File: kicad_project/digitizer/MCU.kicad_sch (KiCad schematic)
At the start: 27 parts, among them J401 Conn_02x05_Odd_Even, U401 ATSAM4E8EA-AN

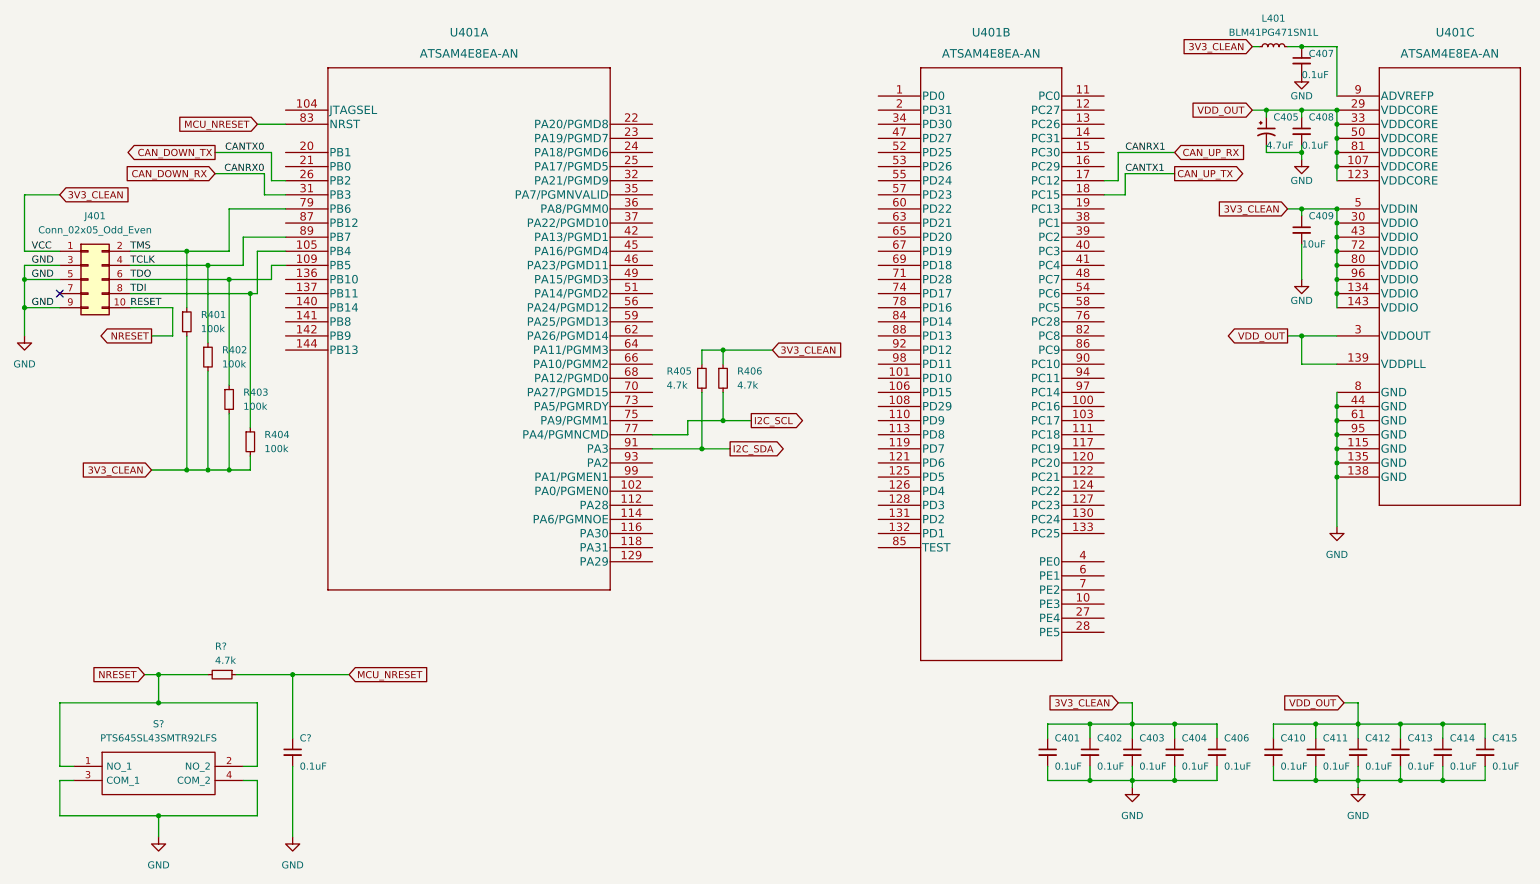
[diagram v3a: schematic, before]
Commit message: added GPIO lines, LED, other small changes
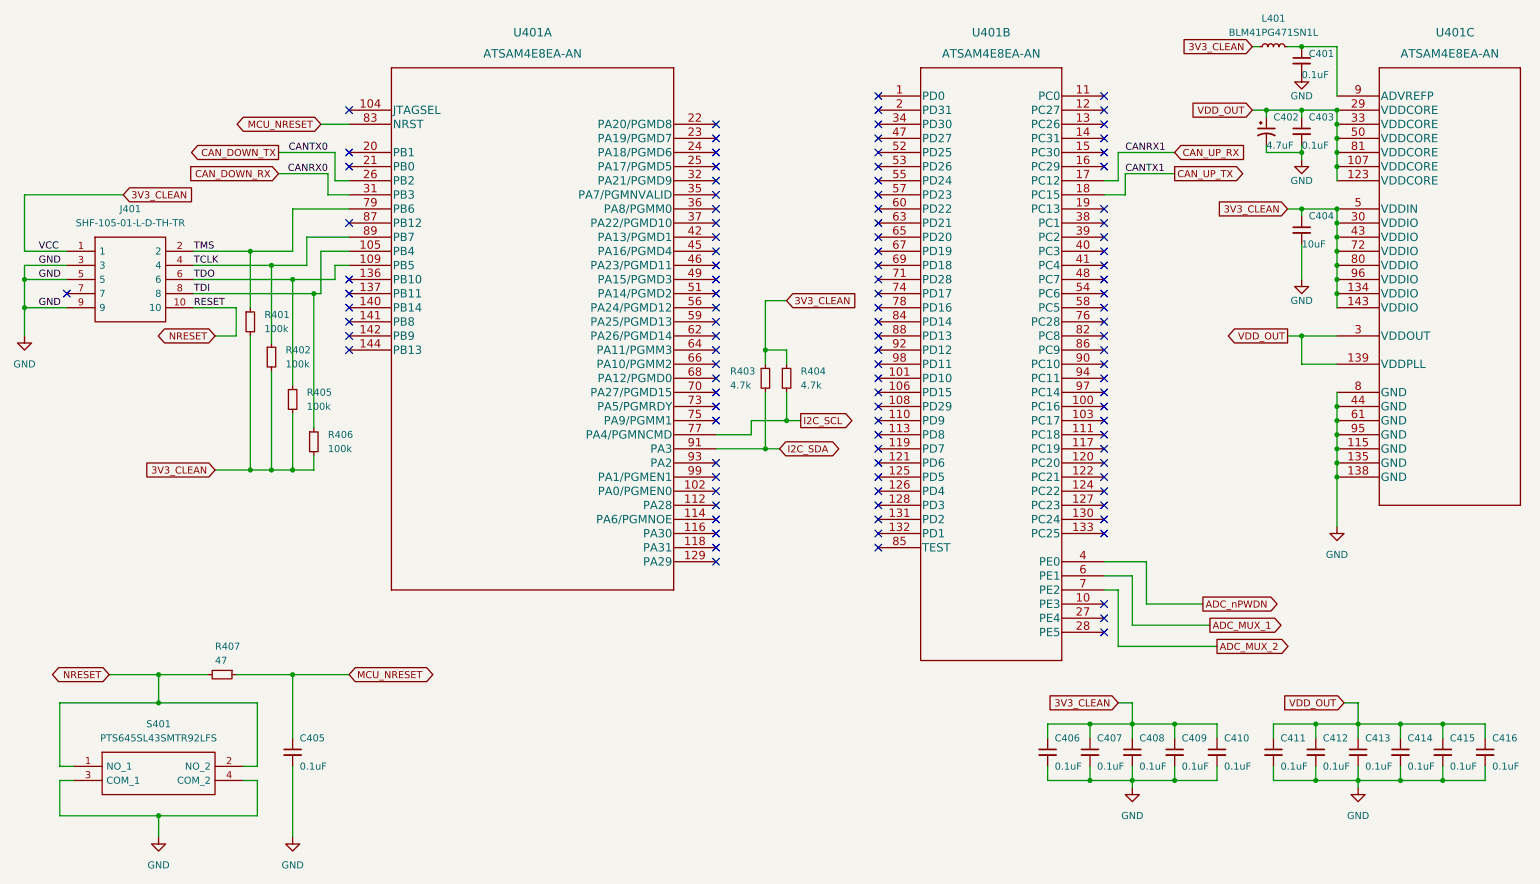
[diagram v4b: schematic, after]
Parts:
- removed J401: Conn_02x05_Odd_Even, SamacSys_Parts:SHF10501LDTHTR, symbol Connector_Generic:Conn_02x05_Odd_Even
- added J401: SHF-105-01-L-D-TH-TR, SHF10501LDTHTR, symbol SamacSys_Parts:SHF-105-01-L-D-TH-TR
- R407: renamed from R?; value 4.7k -> 47
- gave numbers to parts that had none: 2
- renumbered C407 to C401, C405 to C402, C408 to C403, C409 to C404, C401 to C406, C402 to C407, C403 to C408, C404 to C409, C406 to C410, C410 to C411, C411 to C412, C412 to C413, C413 to C414, C414 to C415, C415 to C416, R405 to R403, R406 to R404, R403 to R405, R404 to R406
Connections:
- net 3V3_CLEAN: now also J401.1
- net GND: now also J401.3, J401.5, J401.9
- net NRESET: now also J401.10
- net TCLK: now also J401.4
- net TDI: now also J401.8
- net TDO: now also J401.6
- net TMS: now also J401.2
- net ADC_nPWDN: now reaches U401.4 (PE0)
- net ADC_MUX_1: now reaches U401.6 (PE1)
- net ADC_MUX_2: now reaches U401.7 (PE2)
- no-connect marks 1 -> 107
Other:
- moved on the sheet: R401, R402, R403, R404, R405, R406, U401A

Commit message: updated schematic to include terminal blocks for the analog M12 connectors and the downstream CANPWR connector
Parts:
- J401: footprint SHF10501LDTHTR -> SamacSys_Parts:SHF10501LDTHTR
- U401: footprint LQFP144_20x20MC_MCH -> footprints:ATSAM4E8EA-AN
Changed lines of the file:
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@@
       (effects (font (size 1.524 1.524)))
     )
-    (property "Footprint" "LQFP144_20x20MC_MCH" (id 2) (at 200.66 19.304 0)
+    (property "Footprint" "footprints:ATSAM4E8EA-AN" (id 2) (at 200.66 19.304 0)
       (effects (font (size 1.524 1.524)) hide)
     )
@@
     (property "Reference" "J401" (id 0) (at 33.02 48.26 0))
     (property "Value" "SHF-105-01-L-D-TH-TR" (id 1) (at 33.02 50.8 0))
-    (property "Footprint" "SHF10501LDTHTR" (id 2) (at 40.64 53.34 0)
+    (property "Footprint" "SamacSys_Parts:SHF10501LDTHTR" (id 2) (at 40.64 53.34 0)
       (effects (font (size 1.27 1.27)) (justify left) hide)
     )
@@
       (effects (font (size 1.524 1.524)))
     )
-    (property "Footprint" "LQFP144_20x20MC_MCH" (id 2) (at 105.41 21.844 0)
+    (property "Footprint" "footprints:ATSAM4E8EA-AN" (id 2) (at 105.41 21.844 0)
       (effects (font (size 1.524 1.524)) hide)
     )

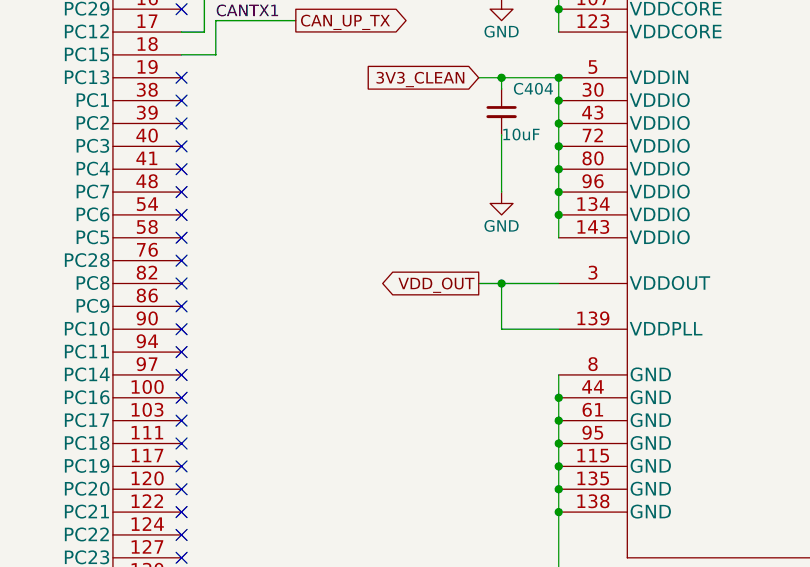
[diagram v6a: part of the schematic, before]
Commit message: cleared ALL errors from electrical rules check; had to explicitly define a bunch of pins, and remove a few bugs (shorted lines, etc.)
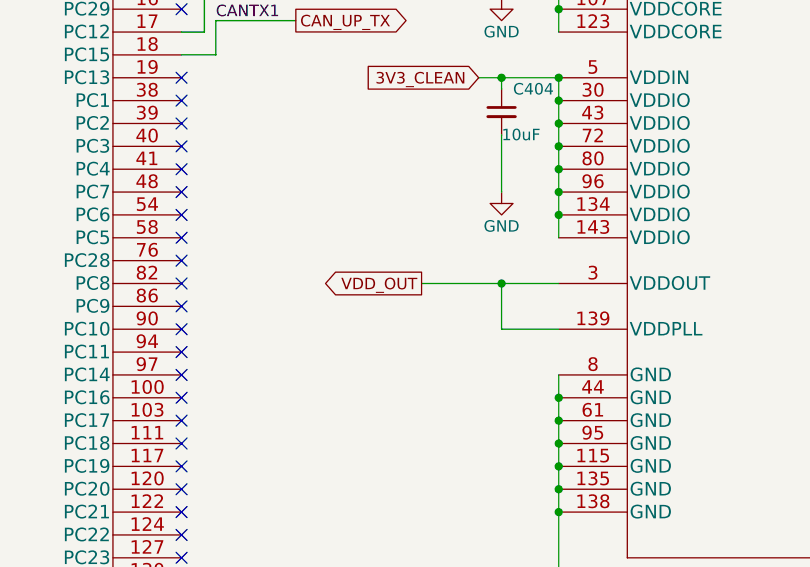
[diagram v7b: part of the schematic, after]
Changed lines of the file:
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@@
   (junction (at 246.38 140.97) (diameter 0) (color 0 0 0 0)
   )
+  (junction (at 220.98 140.97) (diameter 0) (color 0 0 0 0)
+  )
+  (junction (at 261.62 140.97) (diameter 0) (color 0 0 0 0)
+  )
+  (junction (at 237.49 30.48) (diameter 0) (color 0 0 0 0)
+  )
+  (junction (at 151.13 86.36) (diameter 0) (color 0 0 0 0)
+  )
+  (junction (at 261.62 151.13) (diameter 0) (color 0 0 0 0)
+  )
+  (junction (at 250.19 35.56) (diameter 0) (color 0 0 0 0)
+  )
+  (junction (at 147.32 91.44) (diameter 0) (color 0 0 0 0)
+  )
+  (junction (at 250.19 83.82) (diameter 0) (color 0 0 0 0)
+  )
+  (junction (at 58.42 58.42) (diameter 0) (color 0 0 0 0)
+  )
+  (junction (at 250.19 38.1) (diameter 0) (color 0 0 0 0)
+  )
+  (junction (at 250.19 53.34) (diameter 0) (color 0 0 0 0)
+  )
+  (junction (at 269.24 151.13) (diameter 0) (color 0 0 0 0)
+  )
+  (junction (at 220.98 151.13) (diameter 0) (color 0 0 0 0)
+  )
+  (junction (at 147.32 73.66) (diameter 0) (color 0 0 0 0)
+  )
+  (junction (at 250.19 91.44) (diameter 0) (color 0 0 0 0)
+  )
+  (junction (at 62.23 95.25) (diameter 0) (color 0 0 0 0)
+  )
+  (junction (at 13.97 60.96) (diameter 0) (color 0 0 0 0)
+  )
+  (junction (at 13.97 66.04) (diameter 0) (color 0 0 0 0)
+  )
+  (junction (at 205.74 151.13) (diameter 0) (color 0 0 0 0)
+  )
+  (junction (at 250.19 33.02) (diameter 0) (color 0 0 0 0)
+  )
+  (junction (at 54.61 95.25) (diameter 0) (color 0 0 0 0)
+  )
+  (junction (at 243.84 38.1) (diameter 0) (color 0 0 0 0)
+  )
+  (junction (at 250.19 93.98) (diameter 0) (color 0 0 0 0)
+  )
+  (junction (at 250.19 58.42) (diameter 0) (color 0 0 0 0)
+  )
+  (junction (at 250.19 86.36) (diameter 0) (color 0 0 0 0)
+  )
+  (junction (at 54.61 55.88) (diameter 0) (color 0 0 0 0)
+  )
+  (junction (at 250.19 60.96) (diameter 0) (color 0 0 0 0)
+  )
+  (junction (at 205.74 140.97) (diameter 0) (color 0 0 0 0)
+  )
+  (junction (at 66.04 63.5) (diameter 0) (color 0 0 0 0)
+  )
   (junction (at 243.84 19.05) (diameter 0) (color 0 0 0 0)
-  )
-  (junction (at 220.98 140.97) (diameter 0) (color 0 0 0 0)
-  )
-  (junction (at 261.62 140.97) (diameter 0) (color 0 0 0 0)
-  )
-  (junction (at 237.49 30.48) (diameter 0) (color 0 0 0 0)
-  )
-  (junction (at 151.13 86.36) (diameter 0) (color 0 0 0 0)
-  )
-  (junction (at 261.62 151.13) (diameter 0) (color 0 0 0 0)
-  )
-  (junction (at 250.19 35.56) (diameter 0) (color 0 0 0 0)
-  )
-  (junction (at 147.32 91.44) (diameter 0) (color 0 0 0 0)
-  )
-  (junction (at 250.19 83.82) (diameter 0) (color 0 0 0 0)
-  )
-  (junction (at 58.42 58.42) (diameter 0) (color 0 0 0 0)
-  )
-  (junction (at 250.19 38.1) (diameter 0) (color 0 0 0 0)
-  )
-  (junction (at 250.19 53.34) (diameter 0) (color 0 0 0 0)
-  )
-  (junction (at 269.24 151.13) (diameter 0) (color 0 0 0 0)
-  )
-  (junction (at 220.98 151.13) (diameter 0) (color 0 0 0 0)
-  )
-  (junction (at 147.32 73.66) (diameter 0) (color 0 0 0 0)
-  )
-  (junction (at 250.19 91.44) (diameter 0) (color 0 0 0 0)
-  )
-  (junction (at 62.23 95.25) (diameter 0) (color 0 0 0 0)
-  )
-  (junction (at 13.97 60.96) (diameter 0) (color 0 0 0 0)
-  )
-  (junction (at 13.97 66.04) (diameter 0) (color 0 0 0 0)
-  )
-  (junction (at 205.74 151.13) (diameter 0) (color 0 0 0 0)
-  )
-  (junction (at 250.19 33.02) (diameter 0) (color 0 0 0 0)
-  )
-  (junction (at 54.61 95.25) (diameter 0) (color 0 0 0 0)
-  )
-  (junction (at 243.84 38.1) (diameter 0) (color 0 0 0 0)
-  )
-  (junction (at 250.19 93.98) (diameter 0) (color 0 0 0 0)
-  )
-  (junction (at 250.19 58.42) (diameter 0) (color 0 0 0 0)
-  )
-  (junction (at 250.19 86.36) (diameter 0) (color 0 0 0 0)
-  )
-  (junction (at 54.61 55.88) (diameter 0) (color 0 0 0 0)
-  )
-  (junction (at 250.19 60.96) (diameter 0) (color 0 0 0 0)
-  )
-  (junction (at 205.74 140.97) (diameter 0) (color 0 0 0 0)
-  )
-  (junction (at 66.04 63.5) (diameter 0) (color 0 0 0 0)
   )
   (junction (at 250.19 30.48) (diameter 0) (color 0 0 0 0)
@@
     (stroke (width 0) (type default) (color 0 0 0 0))
   )
-  (wire (pts (xy 241.3 71.12) (xy 243.84 71.12))
-    (stroke (width 0) (type default) (color 0 0 0 0))
-  )
   (wire (pts (xy 13.97 60.96) (xy 21.59 60.96))
     (stroke (width 0) (type default) (color 0 0 0 0))
@@
     (stroke (width 0) (type default) (color 0 0 0 0))
   )
+  (wire (pts (xy 241.3 19.05) (xy 243.84 19.05))
+    (stroke (width 0) (type default) (color 0 0 0 0))
+  )
   (wire (pts (xy 237.49 30.48) (xy 243.84 30.48))
     (stroke (width 0) (type default) (color 0 0 0 0))
@@
     (stroke (width 0) (type default) (color 0 0 0 0))
   )
+  (wire (pts (xy 234.95 19.05) (xy 236.22 19.05))
+    (stroke (width 0) (type default) (color 0 0 0 0))
+  )
   (wire (pts (xy 213.36 137.16) (xy 213.36 140.97))
     (stroke (width 0) (type default) (color 0 0 0 0))
@@
     (stroke (width 0) (type default) (color 0 0 0 0))
   )
-  (wire (pts (xy 241.3 19.05) (xy 243.84 19.05))
+  (wire (pts (xy 234.95 71.12) (xy 243.84 71.12))
     (stroke (width 0) (type default) (color 0 0 0 0))
   )
@@
   )
   (wire (pts (xy 254 148.59) (xy 254 151.13))
-    (stroke (width 0) (type default) (color 0 0 0 0))
-  )
-  (wire (pts (xy 234.95 19.05) (xy 236.22 19.05))
     (stroke (width 0) (type default) (color 0 0 0 0))
   )
@@
     )
   )
-  (global_label "VDD_OUT" (shape output) (at 241.3 71.12 180) (fields_autoplaced)
+  (global_label "VDD_OUT" (shape output) (at 234.95 71.12 180) (fields_autoplaced)
     (effects (font (size 1.27 1.27)) (justify right))
-    (property "Intersheet References" "${INTERSHEET_REFS}" (id 0) (at 230.6621 71.0406 0)
+    (property "Intersheet References" "${INTERSHEET_REFS}" (id 0) (at 224.3121 71.0406 0)
       (effects (font (size 1.27 1.27)) (justify right) hide)
     )
@@
   )
   (symbol (lib_id "Device:L_Small") (at 238.76 19.05 90) (unit 1)
-    (in_bom yes) (on_board yes) (fields_autoplaced)
+    (in_bom yes) (on_board yes)
     (property "Reference" "L401" (id 0) (at 238.76 13.97 90))
     (property "Value" "BLM41PG471SN1L" (id 1) (at 238.76 16.51 90))
-    (property "Footprint" "Inductor_SMD:L_1806_4516Metric_Pad1.45x1.90mm_HandSolder" (id 2) (at 238.76 19.05 0)
+    (property "Footprint" "Inductor_SMD:L_1806_4516Metric_Pad1.45x1.90mm_HandSolder" (id 2) (at 234.95 15.24 0)
       (effects (font (size 1.27 1.27)) hide)
     )
@@
     (pin "2")
   )
-  (symbol (lib_id "2022-01-19_19-47-49:ATSAM4E8EA-AN") (at 250.19 27.94 0) (unit 3)
+  (symbol (lib_name "ATSAM4E8EA-AN_1") (lib_id "2022-01-19_19-47-49:ATSAM4E8EA-AN") (at 250.19 27.94 0) (unit 3)
     (in_bom yes) (on_board yes)
     (property "Reference" "U401" (id 0) (at 267.97 16.51 0)

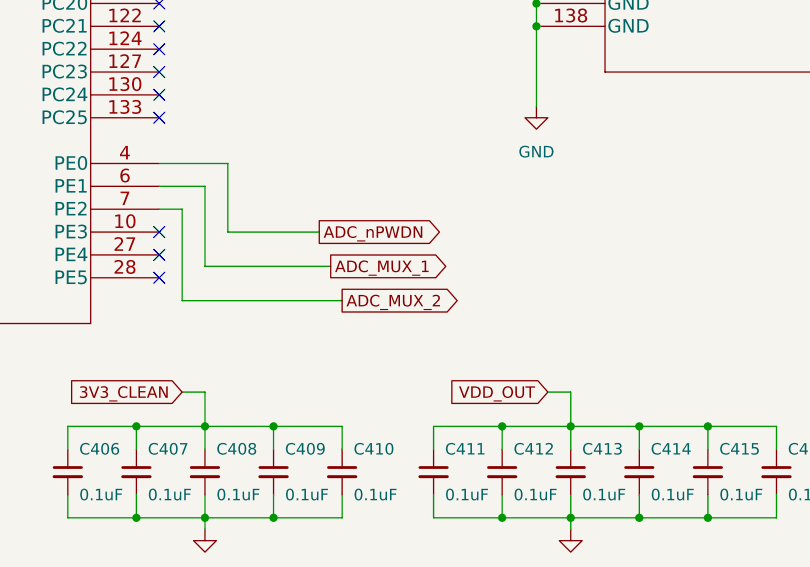
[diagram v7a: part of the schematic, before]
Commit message: fixed another small bug; looks good to begin the board layout!
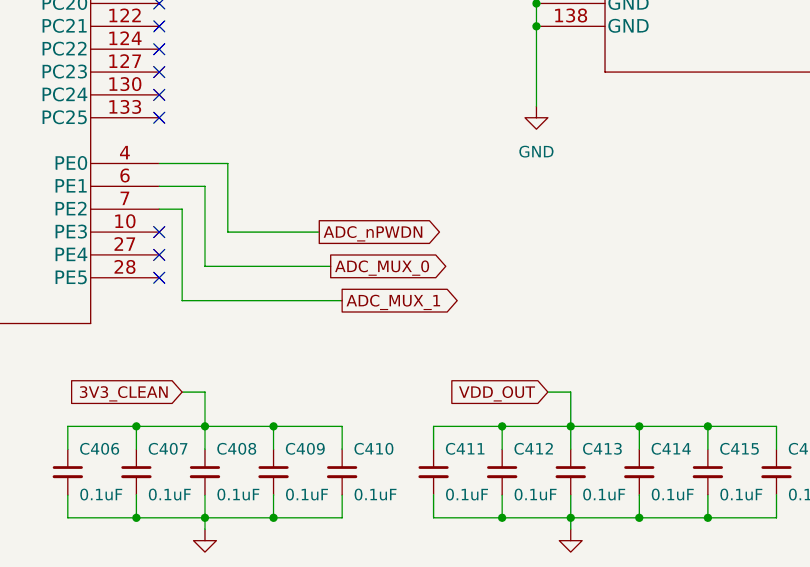
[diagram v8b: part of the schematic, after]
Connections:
- net ADC_MUX_2 is gone; now on net ADC_MUX_1: U401.7 (PE2)
- net ADC_MUX_1: no longer U401.6 (PE1)
- new net ADC_MUX_0: U401.6 (PE1)
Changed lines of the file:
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@@
     )
   )
-  (global_label "ADC_MUX_1" (shape output) (at 227.33 123.19 0) (fields_autoplaced)
+  (global_label "ADC_MUX_0" (shape output) (at 227.33 123.19 0) (fields_autoplaced)
     (effects (font (size 1.27 1.27)) (justify left))
     (property "Intersheet References" "${INTERSHEET_REFS}" (id 0) (at 240.5079 123.1106 0)
@@
     )
   )
-  (global_label "ADC_MUX_2" (shape output) (at 228.6 127 0) (fields_autoplaced)
+  (global_label "ADC_MUX_1" (shape output) (at 228.6 127 0) (fields_autoplaced)
     (effects (font (size 1.27 1.27)) (justify left))
     (property "Intersheet References" "${INTERSHEET_REFS}" (id 0) (at 241.7779 126.9206 0)
